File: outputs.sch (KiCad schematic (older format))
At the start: 68 parts, among them J10 Conn_01x02_Male, J11 NO STUFF, J12 NO STUFF, J2 USB_B_Micro, J3 NO STUFF, J4 HDMI_A_1.4, J5 FH26W-45S-0.3SHW(60), J6 Conn_02x20_Odd_Even, J7 Conn_02x03_Odd_Even, J8 Conn_02x03_Odd_Even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

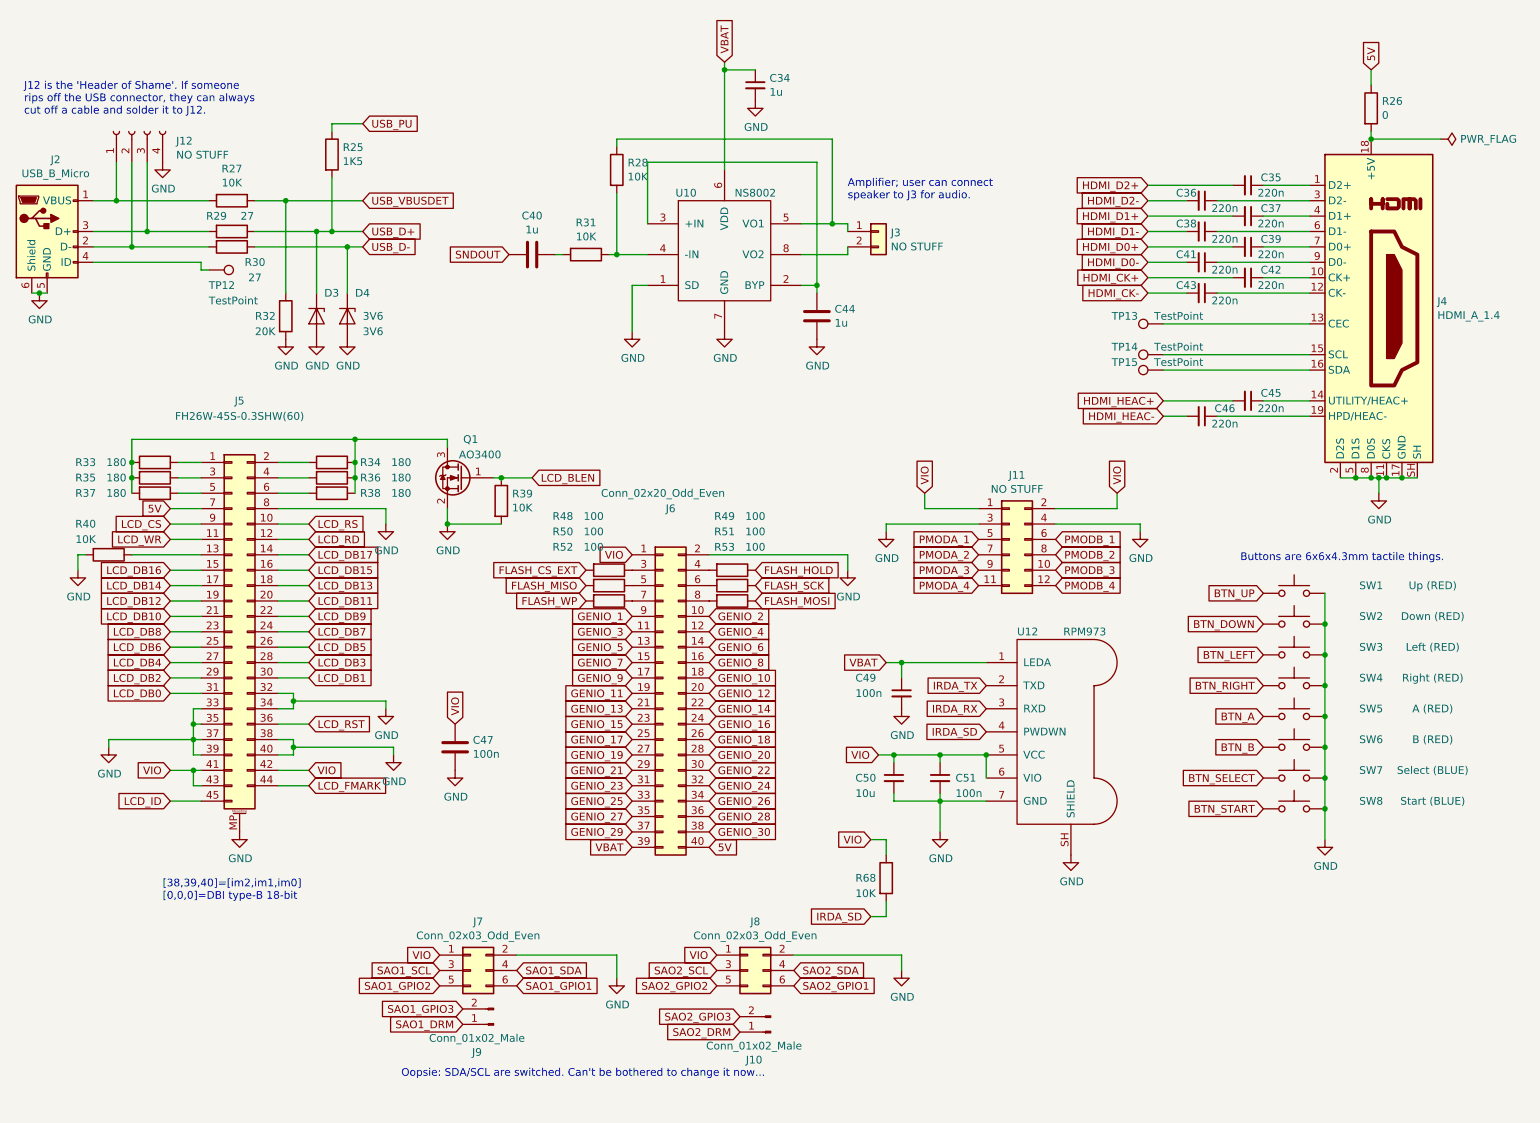
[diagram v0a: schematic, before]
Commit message: Add known issues
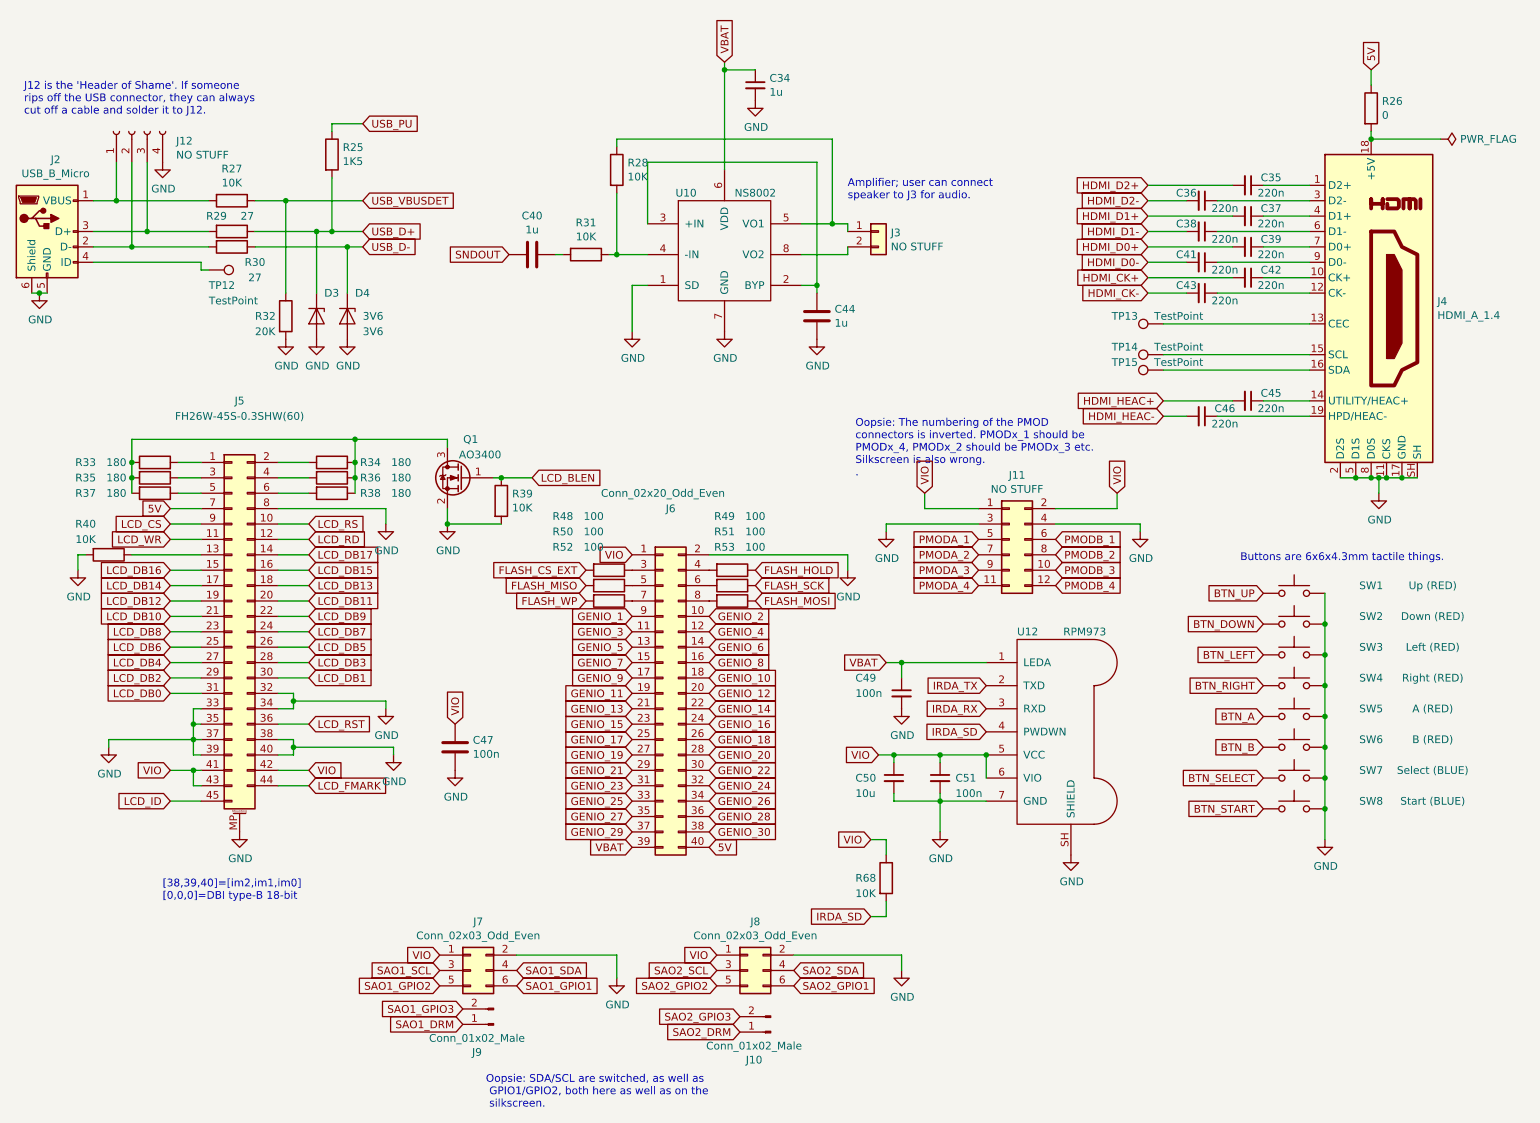
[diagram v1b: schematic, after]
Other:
- note added: "Oopsie: SDA/SCL are switched, as well as\n GPIO1/GPIO2, both here as well as on the\n silkscreen."
- note added: "Oopsie: The numbering of the PMOD\nconnectors is inverted. PMODx_1 should be\nPMODx_4, PMODx_2 should be PMODx_3 etc.\nSilkscreen is also wrong.\n."
- note removed: "Oopsie: SDA/SCL are switched. Can't be bothered to change it now..."
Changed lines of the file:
@@
 Text Notes 9000 4050 0    50   ~ 0
 Buttons are 6x6x4.3mm tactile things.
-Text Notes 3550 7400 0    50   ~ 0
-Oopsie: SDA/SCL are switched. Can't be bothered to change it now...
+Text Notes 4100 7600 0    50   ~ 0
+Oopsie: SDA/SCL are switched, as well as\n GPIO1/GPIO2, both here as well as on the\n silkscreen.
+Text Notes 6500 3500 0    50   ~ 0
+Oopsie: The numbering of the PMOD\nconnectors is inverted. PMODx_1 should be\nPMODx_4, PMODx_2 should be PMODx_3 etc.\nSilkscreen is also wrong.\n.
 $EndSCHEMATC
